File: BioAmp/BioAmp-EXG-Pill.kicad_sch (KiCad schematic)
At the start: 44 parts, among them IC3 MAX1169BEUD+, J1 Conn_01x04_Pin, J2 Conn_01x04_Pin, J3 Conn_01x04_Pin, U1 TL074HIPWR

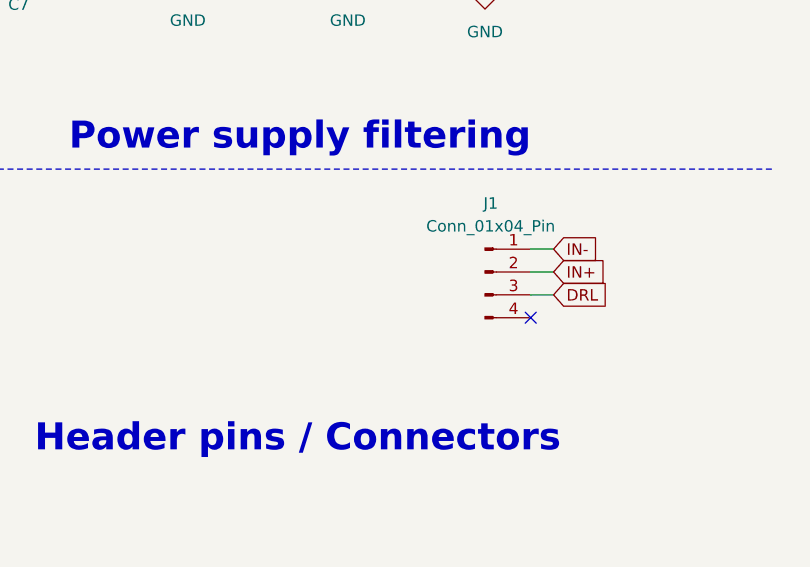
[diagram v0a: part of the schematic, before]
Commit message: Updated FPC connector symbol and footprint
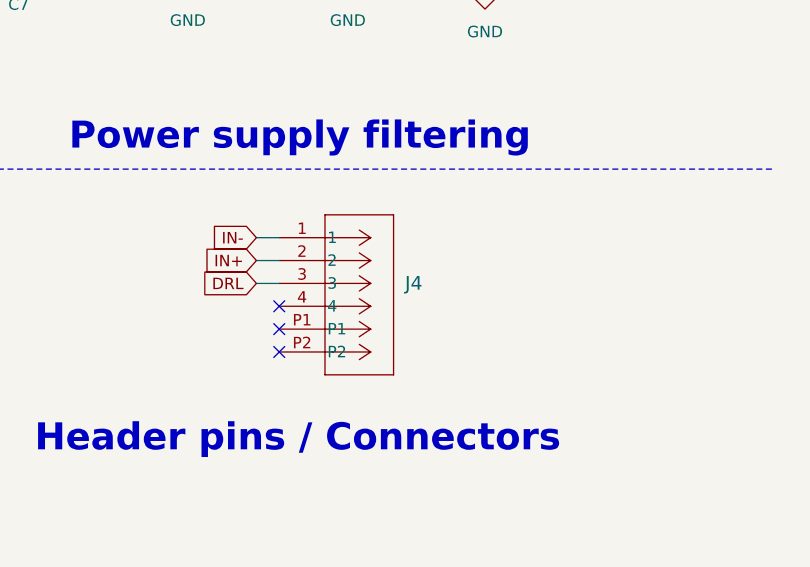
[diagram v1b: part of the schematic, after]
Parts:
- removed J1: Conn_01x04_Pin, Connector_FFC-FPC:Molex_200528-0040_1x04-1MP_P1.00mm_Horizontal, symbol Connector:Conn_01x04_Pin
- added J4: 522710469, CON_522710469_MOL, symbol FPC_Connector:522710469
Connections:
- net DRL: now also J4.3
- net IN+: now also J4.2
- net IN-: now also J4.1
- no-connect marks 1 -> 3
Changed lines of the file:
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@@
 	)
 	(no_connect
-		(at 257.81 149.86)
+		(at 229.87 148.59)
+	)
+	(no_connect
+		(at 229.87 153.67)
+	)
+	(no_connect
+		(at 229.87 151.13)
 	)
 	(wire
@@
 	(wire
 		(pts
+			(xy 227.33 146.05) (xy 229.87 146.05)
+		)
+		(stroke
+			(width 0)
+			(type default)
+		)
+	)
+	(wire
+		(pts
 			(xy 180.34 20.32) (xy 180.34 19.05)
 		)
@@
 	(wire
 		(pts
-			(xy 257.81 144.78) (xy 260.35 144.78)
-		)
-		(stroke
-			(width 0)
-			(type default)
-		)
-	)
-	(wire
-		(pts
 			(xy 30.48 40.64) (xy 31.75 40.64)
 		)
@@
 	(wire
 		(pts
+			(xy 227.33 143.51) (xy 229.87 143.51)
+		)
+		(stroke
+			(width 0)
+			(type default)
+		)
+	)
+	(wire
+		(pts
 			(xy 57.15 29.21) (xy 57.15 35.56)
 		)
@@
 	(wire
 		(pts
-			(xy 257.81 147.32) (xy 260.35 147.32)
-		)
-		(stroke
-			(width 0)
-			(type default)
-		)
-	)
-	(wire
-		(pts
 			(xy 76.2 99.06) (xy 81.28 99.06)
 		)
@@
 	(wire
 		(pts
-			(xy 237.49 87.63) (xy 237.49 99.06)
+			(xy 227.33 140.97) (xy 229.87 140.97)
 		)
 		(stroke
@@
 	(wire
 		(pts
-			(xy 81.28 156.21) (xy 81.28 154.94)
+			(xy 237.49 87.63) (xy 237.49 99.06)
 		)
 		(stroke
@@
 	(wire
 		(pts
-			(xy 254 27.94) (xy 252.73 27.94)
+			(xy 81.28 156.21) (xy 81.28 154.94)
 		)
 		(stroke
@@
 	(wire
 		(pts
-			(xy 190.5 116.84) (xy 190.5 118.11)
+			(xy 254 27.94) (xy 252.73 27.94)
 		)
 		(stroke
@@
 	(wire
 		(pts
-			(xy 257.81 142.24) (xy 260.35 142.24)
+			(xy 190.5 116.84) (xy 190.5 118.11)
 		)
 		(stroke
@@
 		)
 	)
-	(global_label "bpfOUT"
+	(global_label "IN-"
 		(shape input)
-		(at 217.17 25.4 180)
+		(at 227.33 140.97 180)
 		(fields_autoplaced yes)
 		(effects
@@
 		)
 		(property "Intersheetrefs" "${INTERSHEET_REFS}"
-			(at 208.1867 25.4 0)
+			(at 221.4913 140.97 0)
 			(hide yes)
 			(show_name no)
@@
 		)
 	)
-	(global_label "DRL"
+	(global_label "bpfOUT"
 		(shape input)
-		(at 260.35 147.32 0)
+		(at 217.17 25.4 180)
 		(fields_autoplaced yes)
 		(effects
@@
 				(size 1.27 1.27)
 			)
-			(justify left)
+			(justify right)
 		)
 		(property "Intersheetrefs" "${INTERSHEET_REFS}"
-			(at 266.2491 147.32 0)
+			(at 208.1867 25.4 0)
 			(hide yes)
 			(show_name no)
@@
 					(size 1.27 1.27)
 				)
-				(justify left)
+				(justify right)
 			)
 		)
 	)
-	(global_label "inaOUT"
+	(global_label "DRL"
 		(shape input)
-		(at 55.88 105.41 180)
+		(at 227.33 146.05 180)
 		(fields_autoplaced yes)
 		(effects
@@
 		)
 		(property "Intersheetrefs" "${INTERSHEET_REFS}"
-			(at 47.0176 105.41 0)
+			(at 221.4309 146.05 0)
 			(hide yes)
 			(show_name no)
@@
 		)
 	)
-	(global_label "ampRef"
+	(global_label "inaOUT"
 		(shape input)
-		(at 74.93 110.49 180)
+		(at 55.88 105.41 180)
 		(fields_autoplaced yes)
 		(effects
@@
 		)
 		(property "Intersheetrefs" "${INTERSHEET_REFS}"
-			(at 65.5234 110.49 0)
+			(at 47.0176 105.41 0)
 			(hide yes)
 			(show_name no)
@@
 		)
 	)
-	(global_label "IN+"
+	(global_label "ampRef"
 		(shape input)
-		(at 260.35 144.78 0)
+		(at 74.93 110.49 180)
 		(fields_autoplaced yes)
 		(effects
@@
 				(size 1.27 1.27)
 			)
-			(justify left)
+			(justify right)
 		)
 		(property "Intersheetrefs" "${INTERSHEET_REFS}"
-			(at 266.1887 144.78 0)
+			(at 65.5234 110.49 0)
 			(hide yes)
 			(show_name no)
@@
 					(size 1.27 1.27)
 				)
-				(justify left)
+				(justify right)
 			)
 		)
@@
 	(global_label "IN+"
 		(shape input)
+		(at 227.33 143.51 180)
+		(fields_autoplaced yes)
+		(effects
+			(font
+				(size 1.27 1.27)
+			)
+			(justify right)
+		)
+		(property "Intersheetrefs" "${INTERSHEET_REFS}"
+			(at 221.4913 143.51 0)
+			(hide yes)
+			(show_name no)
+			(do_not_autoplace no)
+			(effects
+				(font
+					(size 1.27 1.27)
+				)
+				(justify right)
+			)
+		)
+	)
+	(global_label "IN+"
+		(shape input)
 		(at 71.12 43.18 180)
 		(fields_autoplaced yes)
@@
 		)
 	)
-	(global_label "IN-"
-		(shape input)
-		(at 260.35 142.24 0)
-		(fields_autoplaced yes)
-		(effects
-			(font
-				(size 1.27 1.27)
-			)
-			(justify left)
-		)
-		(property "Intersheetrefs" "${INTERSHEET_REFS}"
-			(at 266.1887 142.24 0)
-			(hide yes)
-			(show_name no)
-			(do_not_autoplace no)
-			(effects
-				(font
-					(size 1.27 1.27)
-				)
-				(justify left)
-			)
-		)
-	)
 	(global_label "DRL"
 		(shape input)
@@
 	)
 	(symbol
-		(lib_id "Connector:Conn_01x04_Pin")
-		(at 252.73 144.78 0)
-		(unit 1)
-		(body_style 1)
-		(exclude_from_sim no)
-		(in_bom yes)
-		(on_board yes)
-		(in_pos_files yes)
-		(dnp no)
-		(fields_autoplaced yes)
-		(property "Reference" "J1"
-			(at 253.365 137.16 0)
-			(show_name no)
-			(do_not_autoplace no)
-			(effects
-				(font
-					(size 1.27 1.27)
-				)
-			)
-		)
-		(property "Value" "Conn_01x04_Pin"
-			(at 253.365 139.7 0)
-			(show_name no)
-			(do_not_autoplace no)
-			(effects
-				(font
-					(size 1.27 1.27)
-				)
-			)
-		)
-		(property "Footprint" "Connector_FFC-FPC:Molex_200528-0040_1x04-1MP_P1.00mm_Horizontal"
-			(at 252.73 144.78 0)
-			(hide yes)
-			(show_name no)
-			(do_not_autoplace no)
-			(effects
-				(font
-					(size 1.27 1.27)
-				)
-			)
-		)
-		(property "Datasheet" ""
-			(at 252.73 144.78 0)
-			(hide yes)
-			(show_name no)
-			(do_not_autoplace no)
-			(effects
-				(font
-					(size 1.27 1.27)
-				)
-			)
-		)
-		(property "Description" "Generic connector, single row, 01x04, script generated"
-			(at 252.73 144.78 0)
-			(hide yes)
-			(show_name no)
-			(do_not_autoplace no)
-			(effects
-				(font
-					(size 1.27 1.27)
-				)
-			)
-		)
-		(pin "4"
-		)
-		(pin "2"
-		)
-		(pin "3"
-		)
-		(pin "1"
-		)
-		(instances
-			(project "BioAmp-EXG-Pill"
-				(path "/6820f13c-3971-4615-b87b-c2f927031906"
-					(reference "J1")
-					(unit 1)
-				)
-			)
-		)
-	)
-	(symbol
 		(lib_id "Device:D_Zener")
 		(at 114.3 167.64 270)
@@
 					(unit 1)
 				)
+			)
+		)
+	)
+	(symbol
+		(lib_id "FPC_Connector:522710469")
+		(at 229.87 140.97 0)
+		(unit 1)
+		(body_style 1)
+		(exclude_from_sim no)
+		(in_bom yes)
+		(on_board yes)
+		(in_pos_files yes)
+		(dnp no)
+		(fields_autoplaced yes)
+		(property "Reference" "J4"
+			(at 243.84 146.0499 0)
+			(show_name no)
+			(do_not_autoplace no)
+			(effects
+				(font
+					(size 1.524 1.524)
+				)
+				(justify left)
+			)
+		)
+		(property "Value" "522710469"
+			(at 243.84 148.5899 0)
+			(hide yes)
+			(show_name no)
+			(do_not_autoplace no)
+			(effects
+				(font
+					(size 1.524 1.524)
+				)
+				(justify left)
+			)
+		)
+		(property "Footprint" "CON_522710469_MOL"
+			(at 229.87 140.97 0)
+			(hide yes)
+			(show_name no)
+			(do_not_autoplace no)
+			(effects
+				(font
+					(size 1.27 1.27)
+					(italic yes)
+				)
+			)
+		)
+		(property "Datasheet" "https://www.molex.com/en-us/products/part-detail-pdf/522710469?display=pdf"
+			(at 229.87 140.97 0)
+			(hide yes)
+			(show_name no)
+			(do_not_autoplace no)
+			(effects
+				(font
+					(size 1.27 1.27)
+					(italic yes)
+				)
+			)
+		)
+		(property "Description" ""
+			(at 229.87 140.97 0)
+			(hide yes)
+			(show_name no)
+			(do_not_autoplace no)
+			(effects
+				(font
+					(size 1.27 1.27)
+				)
+			)
+		)
+		(pin "P1"
+		)
+		(pin "P2"
+		)
+		(pin "4"
+		)
+		(pin "1"
+		)
+		(pin "2"
+		)
+		(pin "3"
+		)
+		(instances
+			(project "BioAmp-EXG-Pill"
+				(path "/6820f13c-3971-4615-b87b-c2f927031906"
+					(reference "J4")
+					(unit 1)
+				)

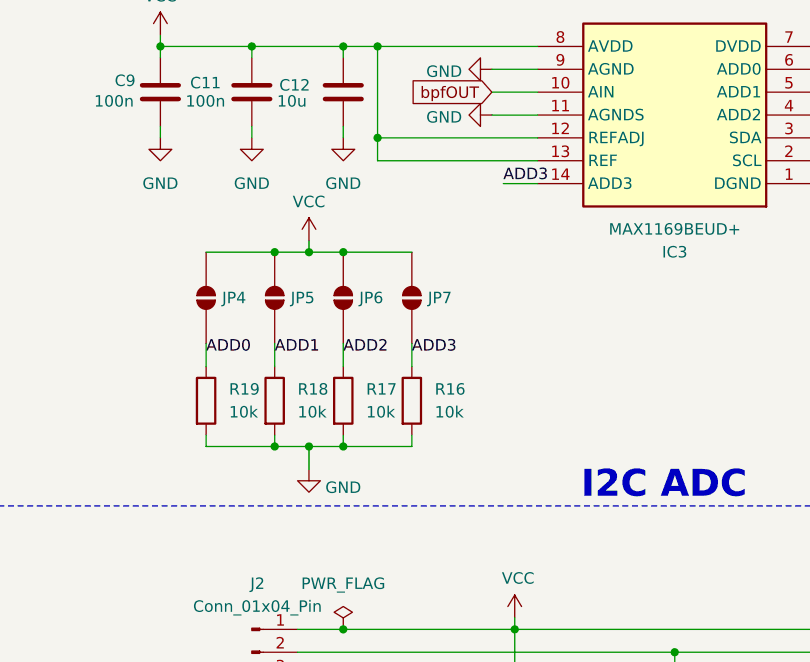
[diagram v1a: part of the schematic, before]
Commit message: Added board constraints
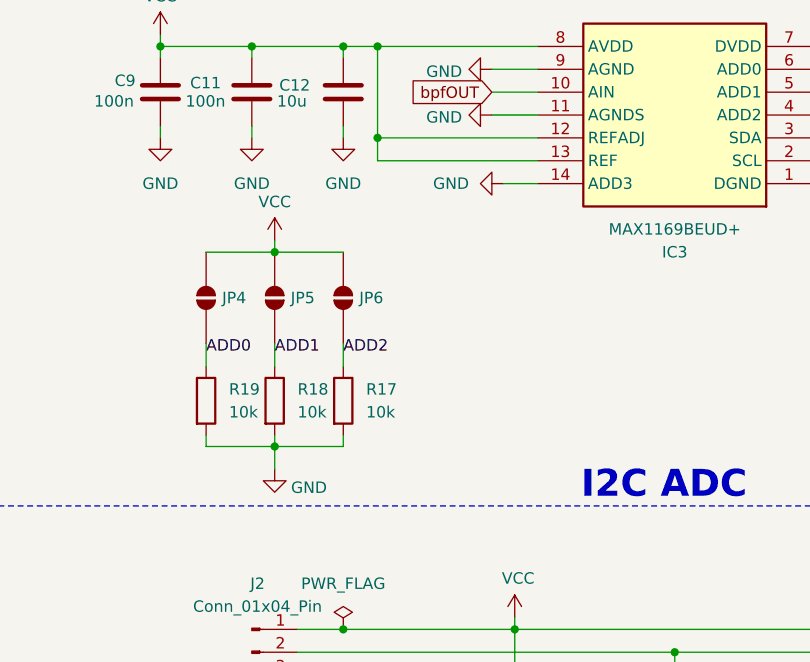
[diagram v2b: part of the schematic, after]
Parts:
- removed JP7: SolderJumper_2_Open, Jumper:SolderJumper-2_P1.3mm_Open_RoundedPad1.0x1.5mm, symbol Jumper:SolderJumper_2_Open
- removed R16: 10k, Resistor_SMD:R_0402_1005Metric, symbol Device:R
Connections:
- net ADD3 is gone; now on net GND: IC3.14 (ADD3)
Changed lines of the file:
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@@
 	)
 	(junction
-		(at 200.66 43.18)
-		(diameter 0)
-		(color 0 0 0 0)
-	)
-	(junction
 		(at 93.98 107.95)
 		(diameter 0)
@@
 	)
 	(junction
-		(at 196.85 43.18)
-		(diameter 0)
-		(color 0 0 0 0)
-	)
-	(junction
 		(at 204.47 20.32)
 		(diameter 0)
@@
 		(color 0 0 0 0)
 	)
-	(junction
-		(at 196.85 64.77)
-		(diameter 0)
-		(color 0 0 0 0)
-	)
-	(junction
-		(at 200.66 64.77)
-		(diameter 0)
-		(color 0 0 0 0)
-	)
 	(no_connect
 		(at 229.87 148.59)
@@
 	(wire
 		(pts
-			(xy 193.04 43.18) (xy 196.85 43.18)
-		)
-		(stroke
-			(width 0)
-			(type default)
-		)
-	)
-	(wire
-		(pts
 			(xy 212.09 92.71) (xy 257.81 92.71)
 		)
@@
 	(wire
 		(pts
-			(xy 196.85 64.77) (xy 196.85 67.31)
+			(xy 193.04 64.77) (xy 193.04 67.31)
 		)
 		(stroke
@@
 	(wire
 		(pts
-			(xy 196.85 43.18) (xy 200.66 43.18)
-		)
-		(stroke
-			(width 0)
-			(type default)
-		)
-	)
-	(wire
-		(pts
 			(xy 71.12 43.18) (xy 72.39 43.18)
 		)
@@
 	(wire
 		(pts
-			(xy 208.28 63.5) (xy 208.28 64.77)
-		)
-		(stroke
-			(width 0)
-			(type default)
-		)
-	)
-	(wire
-		(pts
 			(xy 62.23 29.21) (xy 57.15 29.21)
 		)
@@
 	(wire
 		(pts
-			(xy 196.85 41.91) (xy 196.85 43.18)
+			(xy 193.04 41.91) (xy 193.04 43.18)
 		)
 		(stroke
@@
 	(wire
 		(pts
-			(xy 193.04 64.77) (xy 196.85 64.77)
-		)
-		(stroke
-			(width 0)
-			(type default)
-		)
-	)
-	(wire
-		(pts
 			(xy 107.95 29.21) (xy 113.03 29.21)
 		)
@@
 	(wire
 		(pts
-			(xy 196.85 64.77) (xy 200.66 64.77)
-		)
-		(stroke
-			(width 0)
-			(type default)
-		)
-	)
-	(wire
-		(pts
 			(xy 57.15 105.41) (xy 55.88 105.41)
 		)
@@
 	(wire
 		(pts
-			(xy 208.28 53.34) (xy 208.28 55.88)
-		)
-		(stroke
-			(width 0)
-			(type default)
-		)
-	)
-	(wire
-		(pts
 			(xy 81.28 83.82) (xy 76.2 83.82)
 		)
@@
 	(wire
 		(pts
+			(xy 193.04 43.18) (xy 200.66 43.18)
+		)
+		(stroke
+			(width 0)
+			(type default)
+		)
+	)
+	(wire
+		(pts
 			(xy 81.28 156.21) (xy 81.28 154.94)
 		)
@@
 	(wire
 		(pts
-			(xy 200.66 64.77) (xy 208.28 64.77)
-		)
-		(stroke
-			(width 0)
-			(type default)
-		)
-	)
-	(wire
-		(pts
 			(xy 93.98 83.82) (xy 88.9 83.82)
 		)
@@
 	(wire
 		(pts
-			(xy 40.64 50.8) (xy 40.64 52.07)
+			(xy 193.04 64.77) (xy 200.66 64.77)
 		)
 		(stroke
@@
 	(wire
 		(pts
-			(xy 200.66 43.18) (xy 208.28 43.18)
+			(xy 40.64 50.8) (xy 40.64 52.07)
 		)
 		(stroke
@@
 		)
 	)
-	(label "ADD3"
-		(at 208.28 54.61 0)
-		(effects
-			(font
-				(size 1.27 1.27)
-			)
-			(justify left bottom)
-		)
-	)
 	(label "ADD0"
 		(at 185.42 54.61 0)
@@
 		)
 	)
-	(label "ADD3"
-		(at 218.44 35.56 0)
-		(effects
-			(font
-				(size 1.27 1.27)
-			)
-			(justify left bottom)
-		)
-	)
 	(label "ADD0"
 		(at 254 22.86 0)
@@
 		(lib_name "VCC_1")
 		(lib_id "power:VCC")
-		(at 196.85 41.91 0)
+		(at 193.04 41.91 0)
 		(unit 1)
 		(body_style 1)
@@
 		(dnp no)
 		(property "Reference" "#PWR032"
-			(at 196.85 45.72 0)
+			(at 193.04 45.72 0)
 			(hide yes)
 			(show_name no)
@@
 		)
 		(property "Value" "VCC"
-			(at 196.85 37.592 0)
+			(at 193.04 37.592 0)
 			(show_name no)
 			(do_not_autoplace no)
@@
 		)
 		(property "Footprint" ""
-			(at 196.85 41.91 0)
+			(at 193.04 41.91 0)
 			(hide yes)
 			(show_name no)
@@
 		)
 		(property "Datasheet" ""
-			(at 196.85 41.91 0)
+			(at 193.04 41.91 0)
 			(hide yes)
 			(show_name no)
@@
 		)
 		(property "Description" "Power symbol creates a global label with name \"VCC\""
-			(at 196.85 41.91 0)
+			(at 193.04 41.91 0)
 			(hide yes)
 			(show_name no)
@@
 	)
 	(symbol
-		(lib_id "Device:R")
-		(at 208.28 59.69 0)
-		(unit 1)
-		(body_style 1)
-		(exclude_from_sim no)
-		(in_bom yes)
-		(on_board yes)
-		(in_pos_files yes)
-		(dnp no)
-		(fields_autoplaced yes)
-		(property "Reference" "R16"
-			(at 210.82 58.4199 0)
-			(show_name no)
-			(do_not_autoplace no)
-			(effects
-				(font
-					(size 1.27 1.27)
-				)
-				(justify left)
-			)
-		)
-		(property "Value" "10k"
-			(at 210.82 60.9599 0)
-			(show_name no)
-			(do_not_autoplace no)
-			(effects
-				(font
-					(size 1.27 1.27)
-				)
-				(justify left)
-			)
-		)
-		(property "Footprint" "Resistor_SMD:R_0402_1005Metric"
-			(at 206.502 59.69 90)
-			(hide yes)
-			(show_name no)
-			(do_not_autoplace no)
-			(effects
-				(font
-					(size 1.27 1.27)
-				)
-			)
-		)
-		(property "Datasheet" ""
-			(at 208.28 59.69 0)
-			(hide yes)
-			(show_name no)
-			(do_not_autoplace no)
-			(effects
-				(font
-					(size 1.27 1.27)
-				)
-			)
-		)
-		(property "Description" "Resistor"
-			(at 208.28 59.69 0)
-			(hide yes)
-			(show_name no)
-			(do_not_autoplace no)
-			(effects
-				(font
-					(size 1.27 1.27)
-				)
-			)
-		)
-		(pin "1"
-		)
-		(pin "2"
-		)
-		(instances
-			(project "BioAmp-EXG-Pill"
-				(path "/6820f13c-3971-4615-b87b-c2f927031906"
-					(reference "R16")
-					(unit 1)
-				)
-			)
-		)
-	)
-	(symbol
 		(lib_name "GND_7")
 		(lib_id "power:GND")
@@
 		(lib_name "GND_7")
 		(lib_id "power:GND")
-		(at 196.85 67.31 0)
+		(at 193.04 67.31 0)
 		(unit 1)
 		(body_style 1)
@@
 		(dnp no)
 		(property "Reference" "#PWR033"
-			(at 196.85 73.66 0)
+			(at 193.04 73.66 0)
 			(hide yes)
 			(show_name no)
@@
 		)
 		(property "Value" "GND"
-			(at 200.66 69.342 0)
+			(at 196.85 69.342 0)
 			(show_name no)
 			(do_not_autoplace no)
@@
 		)
 		(property "Footprint" ""
-			(at 196.85 67.31 0)
+			(at 193.04 67.31 0)
 			(hide yes)
 			(show_name no)
@@
 		)
 		(property "Datasheet" ""
-			(at 196.85 67.31 0)
+			(at 193.04 67.31 0)
 			(hide yes)
 			(show_name no)
@@
 		)
 		(property "Description" "Power symbol creates a global label with name \"GND\" , ground"
-			(at 196.85 67.31 0)
+			(at 193.04 67.31 0)
 			(hide yes)
 			(show_name no)
@@
 	)
 	(symbol
-		(lib_id "Jumper:SolderJumper_2_Open")
-		(at 208.28 48.26 90)
+		(lib_name "GND_4")
+		(lib_id "power:GND")
+		(at 218.44 35.56 270)
 		(unit 1)
 		(body_style 1)
 		(exclude_from_sim no)
-		(in_bom no)
+		(in_bom yes)
 		(on_board yes)
 		(in_pos_files yes)
 		(dnp no)
-		(property "Reference" "JP7"
-			(at 210.058 48.26 90)
+		(fields_autoplaced yes)
+		(property "Reference" "#PWR05"
+			(at 212.09 35.56 0)
+			(hide yes)
 			(show_name no)
 			(do_not_autoplace no)
@@
 					(size 1.27 1.27)
 				)
-				(justify right)
 			)
 		)
-		(property "Value" "SolderJumper_2_Open"
-			(at 210.82 49.5299 90)
-			(hide yes)
+		(property "Value" "GND"
+			(at 214.63 35.5599 90)
 			(show_name no)
 			(do_not_autoplace no)
@@
 			)
 		)
-		(property "Footprint" "Jumper:SolderJumper-2_P1.3mm_Open_RoundedPad1.0x1.5mm"
-			(at 208.28 48.26 0)
+		(property "Footprint" ""
+			(at 218.44 35.56 0)
 			(hide yes)
 			(show_name no)
@@
 		)
 		(property "Datasheet" ""
-			(at 215.9 48.26 0)
+			(at 218.44 35.56 0)
 			(hide yes)
 			(show_name no)
@@
 			)
 		)
-		(property "Description" "Solder Jumper, 2-pole, open"
-			(at 213.36 48.26 0)
+		(property "Description" "Power symbol creates a global label with name \"GND\" , ground"
+			(at 218.44 35.56 0)
 			(hide yes)
 			(show_name no)
@@
 		(pin "1"
 		)
-		(pin "2"
-		)
 		(instances
 			(project "BioAmp-EXG-Pill"
 				(path "/6820f13c-3971-4615-b87b-c2f927031906"
-					(reference "JP7")
+					(reference "#PWR05")
 					(unit 1)
 				)

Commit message: Did component placement
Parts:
- C10, C11, C9: footprint Capacitor_SMD:C_0603_1608Metric_Pad1.08x0.95mm_HandSolder -> Capacitor_SMD:C_0402_1005Metric
- J4: footprint CON_522710469_MOL -> FPC_Connector:CON_522710469_MOL
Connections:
- net U1B_in: now reaches R10.2, R7.1, U1.6 (-)
- net U1A_out: now reaches R5.1, R7.2, U1.1
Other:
- moved on the sheet: R7
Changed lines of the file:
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@@
 	)
 	(junction
-		(at 212.09 92.71)
+		(at 95.25 38.1)
 		(diameter 0)
 		(color 0 0 0 0)
 	)
 	(junction
-		(at 190.5 20.32)
+		(at 212.09 92.71)
 		(diameter 0)
 		(color 0 0 0 0)
 	)
 	(junction
-		(at 80.01 43.18)
+		(at 190.5 20.32)
 		(diameter 0)
 		(color 0 0 0 0)
 	)
 	(junction
-		(at 180.34 20.32)
+		(at 80.01 43.18)
 		(diameter 0)
 		(color 0 0 0 0)
 	)
 	(junction
-		(at 95.25 38.1)
+		(at 180.34 20.32)
 		(diameter 0)
 		(color 0 0 0 0)
@@
 	)
 	(junction
-		(at 72.39 38.1)
-		(diameter 0)
-		(color 0 0 0 0)
-	)
-	(junction
 		(at 40.64 40.64)
 		(diameter 0)
@@
 	)
 	(junction
+		(at 72.39 38.1)
+		(diameter 0)
+		(color 0 0 0 0)
+	)
+	(junction
 		(at 204.47 20.32)
 		(diameter 0)
@@
 	(wire
 		(pts
-			(xy 83.82 38.1) (xy 95.25 38.1)
+			(xy 87.63 38.1) (xy 95.25 38.1)
 		)
 		(stroke
@@
 	(wire
 		(pts
-			(xy 76.2 38.1) (xy 72.39 38.1)
+			(xy 80.01 38.1) (xy 72.39 38.1)
 		)
 		(stroke
@@
 		)
 	)
+	(label "U1A_out"
+		(at 72.39 38.1 0)
+		(effects
+			(font
+				(size 0.635 0.635)
+			)
+			(justify left bottom)
+		)
+	)
 	(label "IN-_Prot"
 		(at 49.53 40.64 0)
@@
 		)
 	)
+	(label "U1B_in"
+		(at 88.9 38.1 0)
+		(effects
+			(font
+				(size 0.635 0.635)
+			)
+			(justify left bottom)
+		)
+	)
 	(label "ADD0"
 		(at 254 22.86 0)
@@
 	(symbol
 		(lib_id "Device:R")
-		(at 80.01 38.1 270)
+		(at 83.82 38.1 270)
 		(unit 1)
 		(body_style 1)
@@
 		(dnp no)
 		(property "Reference" "R7"
-			(at 80.01 36.068 90)
+			(at 83.82 36.068 90)
 			(show_name no)
 			(do_not_autoplace no)
@@
 		)
 		(property "Value" "22K"
-			(at 80.264 38.1 90)
+			(at 84.074 38.1 90)
 			(show_name no)
 			(do_not_autoplace no)
@@
 		)
 		(property "Footprint" "Resistor_SMD:R_0603_1608Metric_Pad0.98x0.95mm_HandSolder"
-			(at 80.01 36.322 90)
+			(at 83.82 36.322 90)
 			(hide yes)
 			(show_name no)
@@
 		)
 		(property "Datasheet" ""
-			(at 80.01 38.1 0)
+			(at 83.82 38.1 0)
 			(hide yes)
 			(show_name no)
@@
 		)
 		(property "Description" ""
-			(at 80.01 38.1 0)
+			(at 83.82 38.1 0)
 			(show_name no)
 			(do_not_autoplace no)
@@
 			)
 		)
-		(property "Footprint" "Capacitor_SMD:C_0603_1608Metric_Pad1.08x0.95mm_HandSolder"
+		(property "Footprint" "Capacitor_SMD:C_0402_1005Metric"
 			(at 268.2748 21.59 0)
 			(hide yes)
@@
 			)
 		)
-		(property "Footprint" "Capacitor_SMD:C_0603_1608Metric_Pad1.08x0.95mm_HandSolder"
+		(property "Footprint" "Capacitor_SMD:C_0402_1005Metric"
 			(at 179.3748 21.59 0)
 			(hide yes)
@@
 			)
 		)
-		(property "Footprint" "Capacitor_SMD:C_0603_1608Metric_Pad1.08x0.95mm_HandSolder"
+		(property "Footprint" "Capacitor_SMD:C_0402_1005Metric"
 			(at 189.5348 21.59 0)
 			(hide yes)
@@
 			)
 		)
-		(property "Footprint" "CON_522710469_MOL"
+		(property "Footprint" "FPC_Connector:CON_522710469_MOL"
 			(at 229.87 140.97 0)
 			(hide yes)
